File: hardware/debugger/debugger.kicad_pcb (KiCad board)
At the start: 4 copper layers, 148.6 x 48.3 mm, 23 parts, among them J1 DB37_Male, J2 DB37_Male, U1 Teensy3.6, U10 PI6C49CB04AQ, U11 PI6C49CB04AQ, U2 SN74CBTLV3257PWR, U3 SN74CBTLV3257PWR, U4 SN74CBTLV3257PWR, U5 SN74CBTLV3257PWR, U6 SN74CBTLV3257PWR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

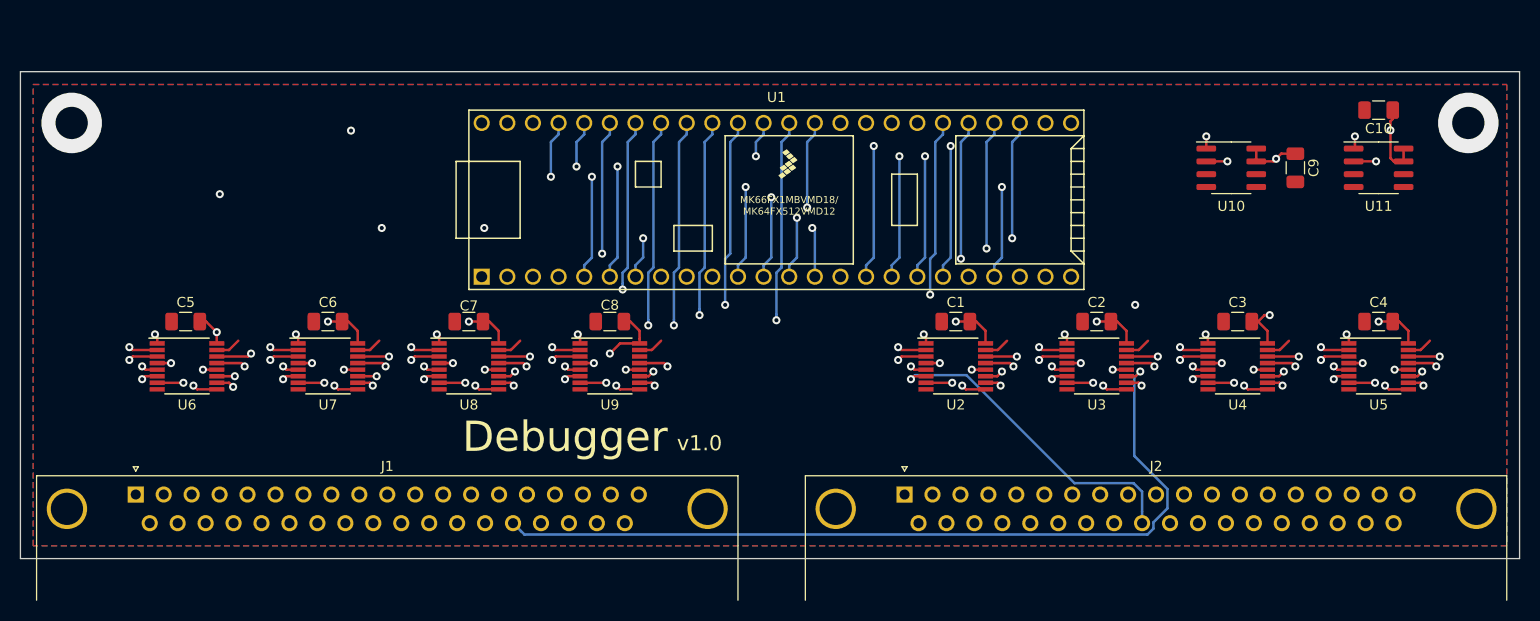
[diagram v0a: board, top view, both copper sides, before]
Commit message: Debugger updates (#10)
* Debugger updated to Teensy 4.1 with magjack for ethernet. Updated motherboard<>debugger pinout to include 3.3v source

* Added 2 mils extra clearance for paste layer

* cleanup
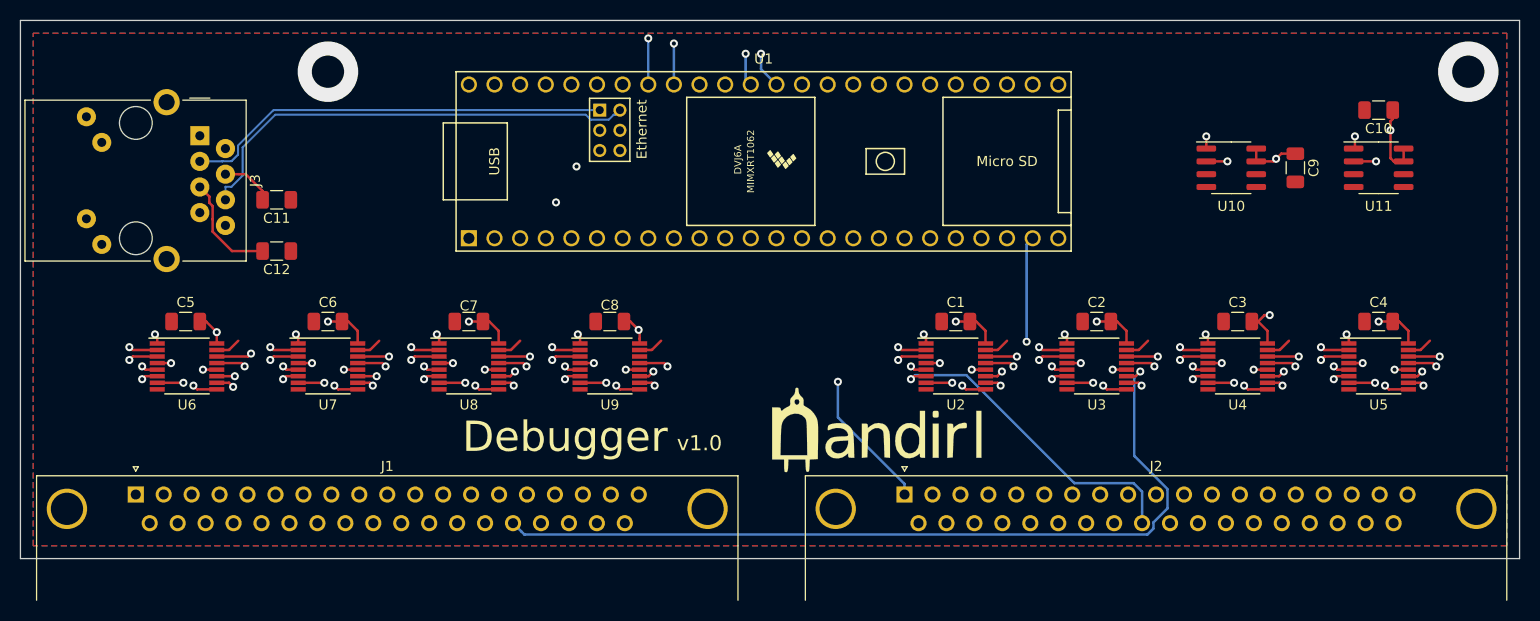
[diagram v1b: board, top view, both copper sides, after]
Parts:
- added C11: 0.1uF, Capacitor_SMD:C_1206_3216Metric, F.Cu at (105.4, 97.8)
- added C12: 0.1uF, Capacitor_SMD:C_1206_3216Metric, F.Cu at (105.4, 102.9)
- added G***: LOGO, nandirl logo:logo_sm, F.Cu at (165.1, 120.7)
- added J3: RJ45_Amphenol_RJMG1BD3B8K1ANR, Connector_RJ:RJ45_Amphenol_RJMG1BD3B8K1ANR, F.Cu at (97.8, 91.4)
- U1: value Teensy3.6 -> Teensy4.1; footprint nandirl logo:Teensy35_36 -> nandirl logo:Teensy41
- moved U1 4.02 mm to (153.7, 94.0)
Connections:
- J2 pad 18: Net-(J2-Pad18) -> +3V3
- J2 pad 37: Net-(J2-Pad37) -> +3V3
- U1 pad 10: inst_dreg3 -> inst_dreg8
- U1 pad 11: pc_aregmem3 -> inst_dreg9
- U1 pad 12: pc_aregmem4 -> inst_dreg10
- U1 pad 13: pc_aregmem6 -> inst_dreg11
- U1 pad 14: pc_aregmem7 -> inst_dreg12
- U1 pad 16: reset -> inst_dreg13
- U1 pad 17: sel_pc_aregmem -> inst_dreg14
- U1 pad 18: inst_dreg14 -> pc_aregmem14
- U1 pad 19: inst_dreg15 -> pc_aregmem15
- U1 pad 2: inst_dreg8 -> inst_dreg0
- U1 pad 20: sel_inst_dreg -> inst_dreg15
- U1 pad 21: inst_dreg10 -> clk_a_pre
- U1 pad 22: inst_dreg11 -> clk_b_pre
- U1 pad 3: inst_dreg9 -> inst_dreg1
- U1 pad 30: clk_a_pre -> pc_aregmem12
- U1 pad 31: clk_b_pre -> pc_aregmem13
- U1 pad 32: pc_aregmem8 -> pc_aregmem4
- U1 pad 33: pc_aregmem9 -> pc_aregmem5
- U1 pad 34: pc_aregmem10 -> GND
- U1 pad 35: pc_aregmem11 -> Net-(U1-Pad35)
- U1 pad 36: Net-(U1-Pad36) -> pc_aregmem2
- U1 pad 37: Net-(U1-Pad37) -> pc_aregmem3
- U1 pad 38: Net-(U1-Pad38) -> pc_aregmem7
- U1 pad 39: GND -> pc_aregmem6
- U1 pad 4: inst_dreg0 -> inst_dreg2
- U1 pad 40: pc_aregmem5 -> pc_aregmem1
- U1 pad 41: inst_dreg1 -> pc_aregmem0
- U1 pad 42: pc_aregmem0 -> pc_aregmem10
- U1 pad 43: pc_aregmem12 -> pc_aregmem11
- U1 pad 44: pc_aregmem13 -> pc_aregmem8
- U1 pad 45: pc_aregmem15 -> pc_aregmem9
- U1 pad 46: pc_aregmem14 -> Net-(U1-Pad46)
- U1 pad 47: inst_dreg5 -> GND
- U1 pad 48: inst_dreg6 -> Net-(U1-Pad48)
- U1 pad 5: inst_dreg12 -> inst_dreg3
- U1 pad 6: inst_dreg13 -> inst_dreg4
- U1 pad 7: inst_dreg7 -> inst_dreg5
- U1 pad 8: inst_dreg4 -> inst_dreg6
- U1 pad 9: inst_dreg2 -> inst_dreg7
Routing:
- net rom_we: track 207.9 -> 44.9 mm, vias 1 -> 2
- net rom_oe: track 131.1 -> 190.3 mm, vias 1 -> 0
- net LED: track 0.00 -> 53.0 mm
- net R-: track 0.00 -> 45.6 mm
- net T+: track 0.00 -> 43.9 mm
- net pc_aregmem8: track 79.6 -> 35.8 mm
- net R+: track 0.00 -> 42.3 mm
- net T-: track 0.00 -> 38.4 mm
- net inst_dreg9: track 101.9 -> 64.5 mm
- net pc_aregmem10: track 77.3 -> 40.3 mm, vias 2 -> 1
- net inst_dreg13: track 99.6 -> 64.4 mm, vias 2 -> 1
- net inst_dreg12: track 95.9 -> 65.4 mm, vias 2 -> 1
- net pc_aregmem11: track 66.6 -> 37.6 mm, vias 2 -> 1
- net inst_dreg11: track 31.5 -> 58.7 mm, vias 2 -> 1
- net inst_dreg8: track 89.3 -> 62.3 mm
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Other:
- board size 148.6 x 48.3 mm -> 148.6 x 53.3 mm
